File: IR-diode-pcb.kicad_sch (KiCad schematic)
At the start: 12 parts, among them U1 MP2483DQ-LF-P

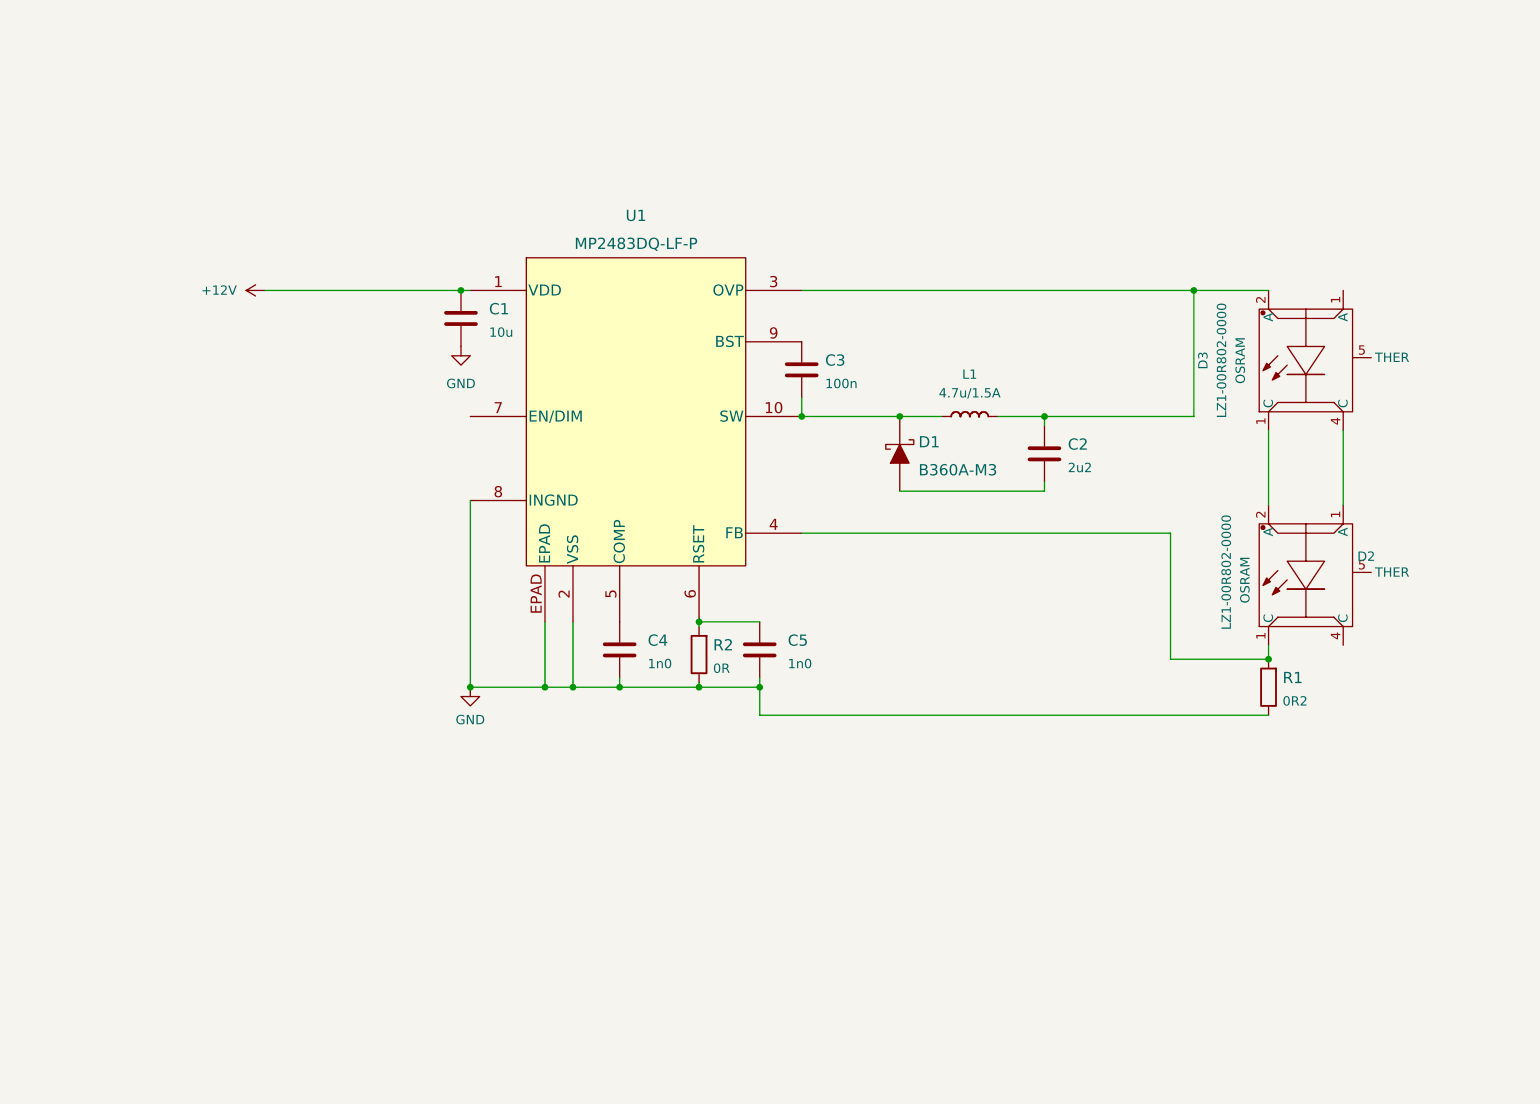
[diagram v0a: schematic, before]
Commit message: Converter configured, pcb started
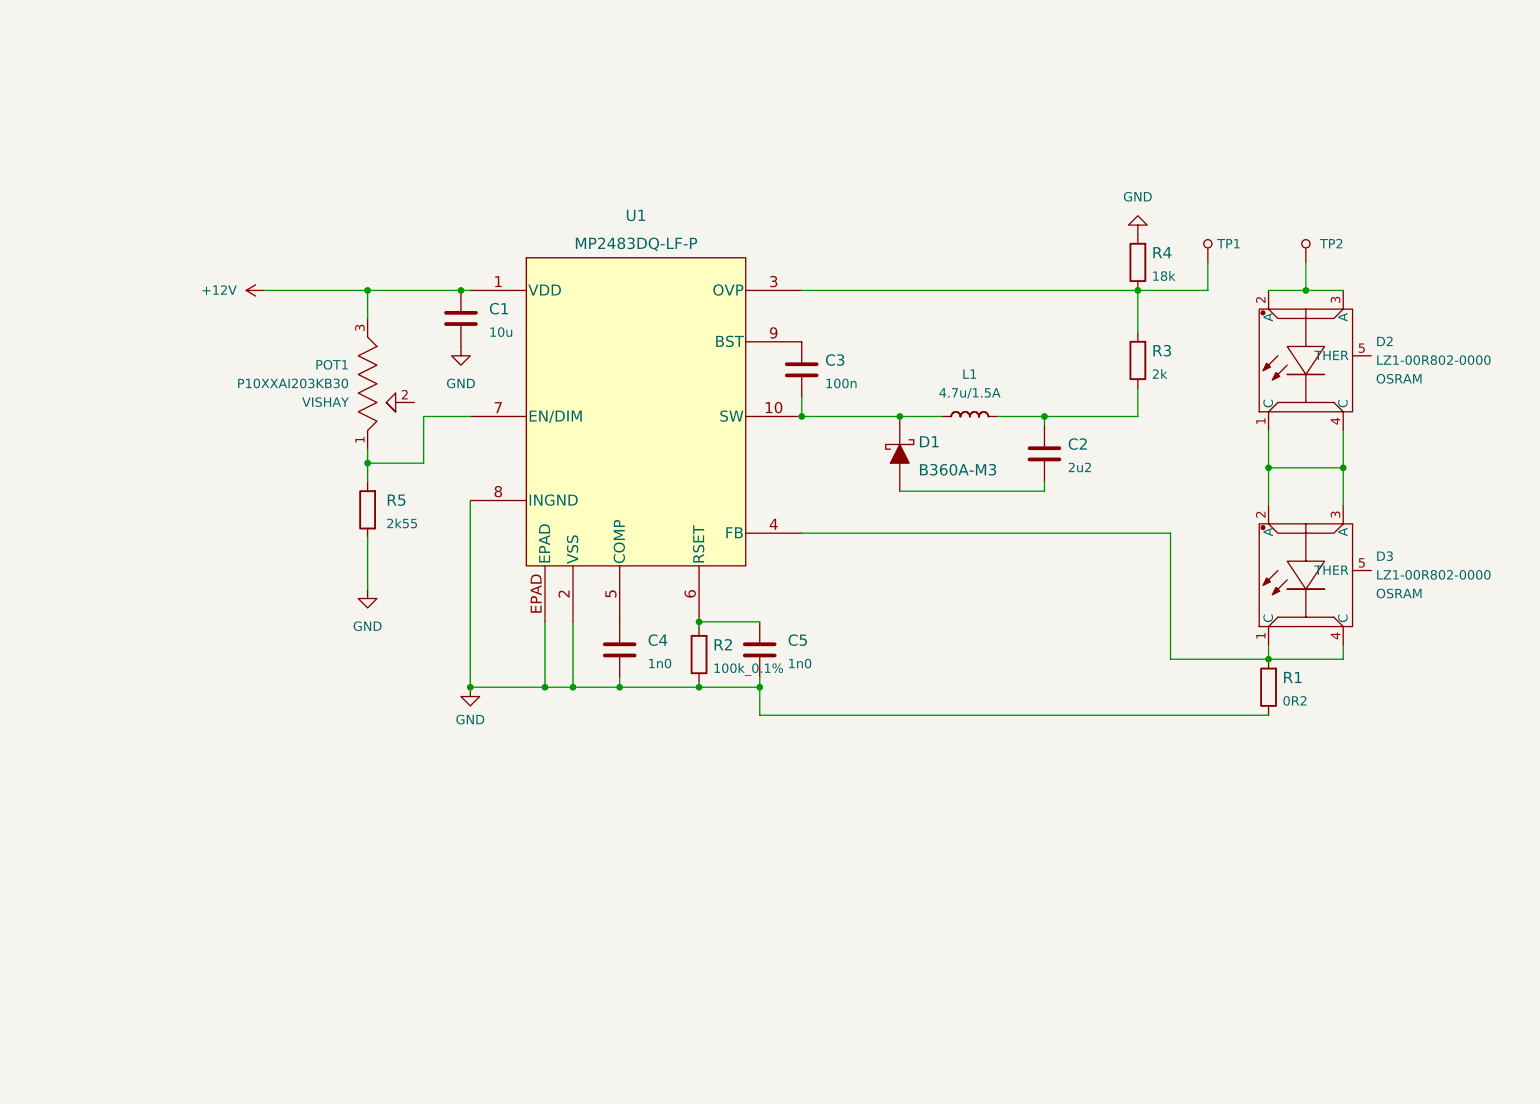
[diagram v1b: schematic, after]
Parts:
- removed R2: R_0R_0402, antmicro-footprints:0402-res, symbol antmicroResistors0402:R_0R_0402
- added POT1: P10XXAI203KB30, antmicro-footprints:P10XXAI203KB30, symbol antmicroRotaryPotentiometersRheostats:P10XXAI203KB30
- added R2: R_100k_0.1%_0402, antmicro-footprints:0402-res, symbol antmicroResistors0402:R_100k_0.1%_0402
- added R3: R_2k_0402, antmicro-footprints:0402-res, symbol antmicroResistors0402:R_2k_0402
- added R4: R_18k_0402, antmicro-footprints:0402-res, symbol antmicroResistors0402:R_18k_0402
- added R5: R_2k55_0402, antmicro-footprints:0402-res, symbol antmicroResistors0402:R_2k55_0402
- added TP1, TP2: 5017, antmicro-footprints:PC_TEST-POINT_MINI_3.43x1.78mm, symbol antmicroTestPoints:5017
- D2, D3: footprint antmicro-footprints:LZ1-00R802-0000 -> antmicro-footprints:LZ1-00R802_4EP_4.4x4.4
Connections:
- net +12V: now also POT1.3
- net GND: now also R2.1, R4.2, R5.1
- net at C2.1, L1.2 (P): now also R3.1; no longer D3.2 (A), U1.3 (OVP)
- net at C5.1, U1.6 (RSET): now also R2.2
- net at R1.2, U1.4 (FB): now also D3.1 (C), D3.4 (C); no longer D2.1 (C)
- net at U1.7 (EN/DIM): now also POT1.1, R5.2
- net at D2.1 (C): now also D2.4 (C), D3.2 (A), D3.3 (A); no longer D3.4 (C)
- net at D2.2 (A): now also D2.3 (A), TP2.1; no longer D3.1 (C)
- new net: R3.2, R4.1, TP1.1, U1.3 (OVP)

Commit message: Added USB-C and power barrel connector
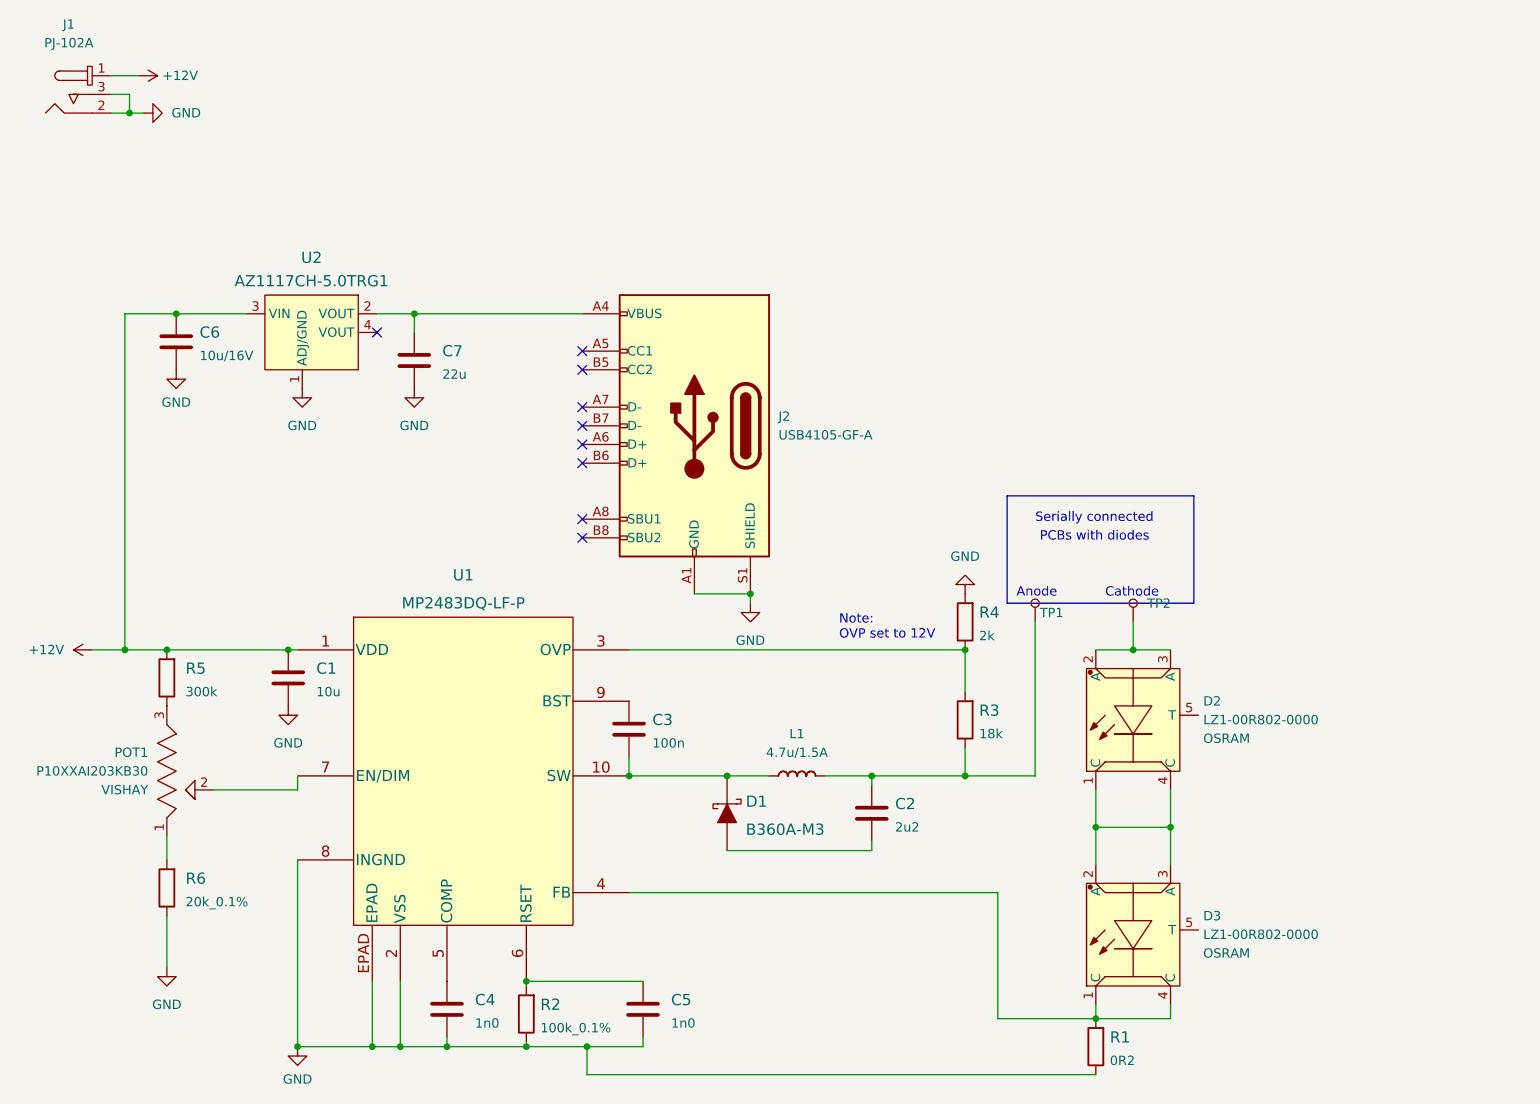
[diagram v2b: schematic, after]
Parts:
- removed C1: C_10u_0402, antmicro-footprints:0402-cap, symbol antmicroCapacitors0402:C_10u_0402
- removed R3: R_2k_0402, antmicro-footprints:0402-res, symbol antmicroResistors0402:R_2k_0402
- removed R4: R_18k_0402, antmicro-footprints:0402-res, symbol antmicroResistors0402:R_18k_0402
- removed R5: R_2k55_0402, antmicro-footprints:0402-res, symbol antmicroResistors0402:R_2k55_0402
- added C1: C_10u_0805, antmicro-footprints:0805-cap, symbol antmicroCapacitorsmisc:C_10u_0805
- added C6: C_10u_16V_0603, antmicro-footprints:0603-cap, symbol antmicroCapacitors0603:C_10u_16V_0603
- added C7: C_22u_0402, antmicro-footprints:0402-cap, symbol antmicroCapacitors0402:C_22u_0402
- added J1: PJ-102A, antmicro-footprints:Barrel_Jack_5.5mmODx2.1mmID_PJ-102A, symbol antmicroBarrelPowerConnectors:PJ-102A
- added J2: USB4105-GF-A, antmicro-footprints:GCT_USB4105-GF-A, symbol antmicroUSBDVIHDMIConnectors:USB4105-GF-A
- added R3: R_18k_0402, antmicro-footprints:0402-res, symbol antmicroResistors0402:R_18k_0402
- added R4: R_2k_0402, antmicro-footprints:0402-res, symbol antmicroResistors0402:R_2k_0402
- added R5: R_300k_0603, antmicro-footprints:0603-res, symbol antmicroResistors0603:R_300k_0603
- added R6: R_20k_0.1%_0402, antmicro-footprints:0402-res, symbol antmicroResistors0402:R_20k_0.1%_0402
- added U2: AZ1117CH-5.0TRG1, antmicro-footprints:SOT-223, symbol antmicroPMICVoltageRegulatorsLinear:AZ1117CH-5.0TRG1
- POT1: footprint antmicro-footprints:P10XXAI203KB30 -> antmicro-footprints:P10XHAI203KB30
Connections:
- net +12V: now also C1.1, C6.1, J1.1, R5.2, U2.3 (VIN); no longer POT1.3
- net GND: now also C1.2, C6.2, C7.2, J1.2, J1.3, J2.A1 (GND), J2.A12 (GND), J2.B1 (GND), J2.B12 (GND), J2.S1 (SHIELD), R4.2, R6.1, U2.1 (ADJ/GND)
- net at POT1.1: now also R6.2; no longer U1.7 (EN/DIM)
- net at POT1.2: now also U1.7 (EN/DIM)
- net at C2.1, L1.2 (P): now also TP1.1, R3.1
- net at U1.3 (OVP): now also R3.2, R4.1; no longer TP1.1
- new net: POT1.3, R5.1
- new net: C7.1, J2.A4 (VBUS), J2.A9 (VBUS), J2.B4 (VBUS), J2.B9 (VBUS), U2.2 (VOUT)
- no-connect marks 0 -> 9
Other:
- note added: "Anode"
- note added: "Cathode"
- note added: "Note: OVP set to 12V"
- note added: "PCBs with diodes"
- note added: "Serially connected"
- moved on the sheet: C2, C3, C4, C5, D1, L1, POT1, R1, R2, TP1, TP2, U1
